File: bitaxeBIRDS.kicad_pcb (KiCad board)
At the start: 6 copper layers, 65 x 120 mm, 198 parts, among them J1 XT30, J4 Conn_01x04, Q1 BSS138, U12 TLV75512PDQNR, U14 TLV75512PDQNR, U15 TLV75512PDQNR, U2 TPS546D24SRVFR, U3 TLV75512PDQNR, U5 TPS22919DCKR, U8 SN74AXC4T774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

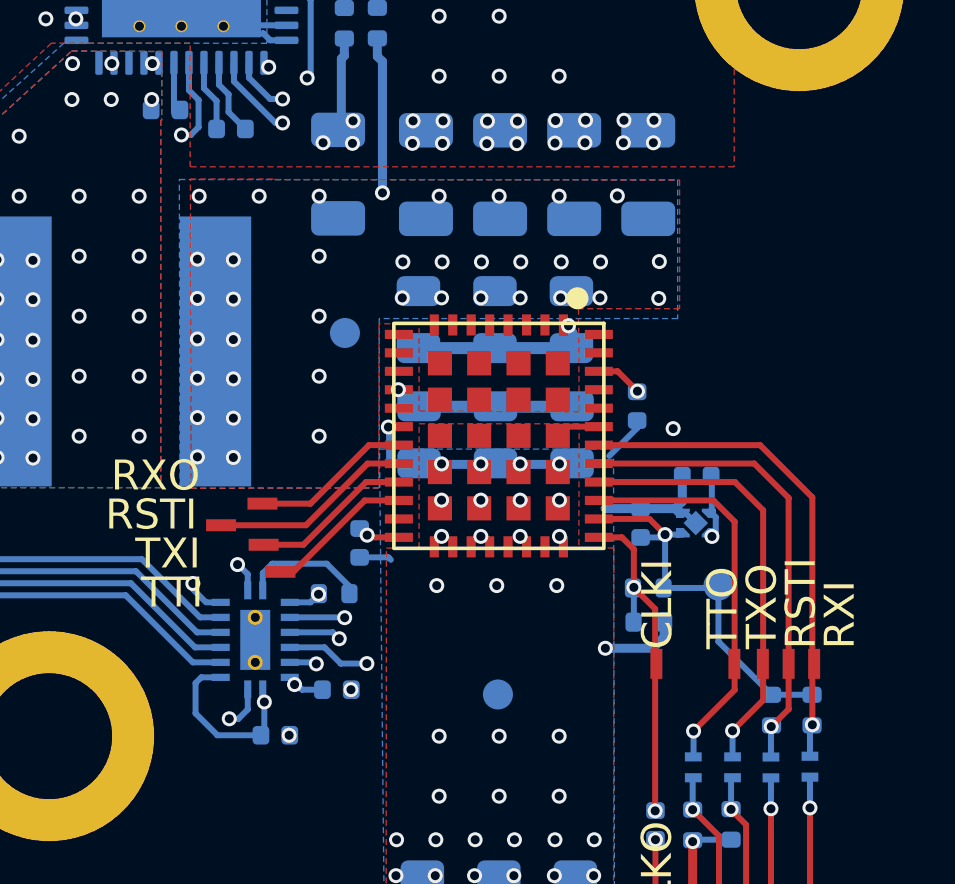
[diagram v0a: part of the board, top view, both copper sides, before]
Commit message: added pull resistors for #1
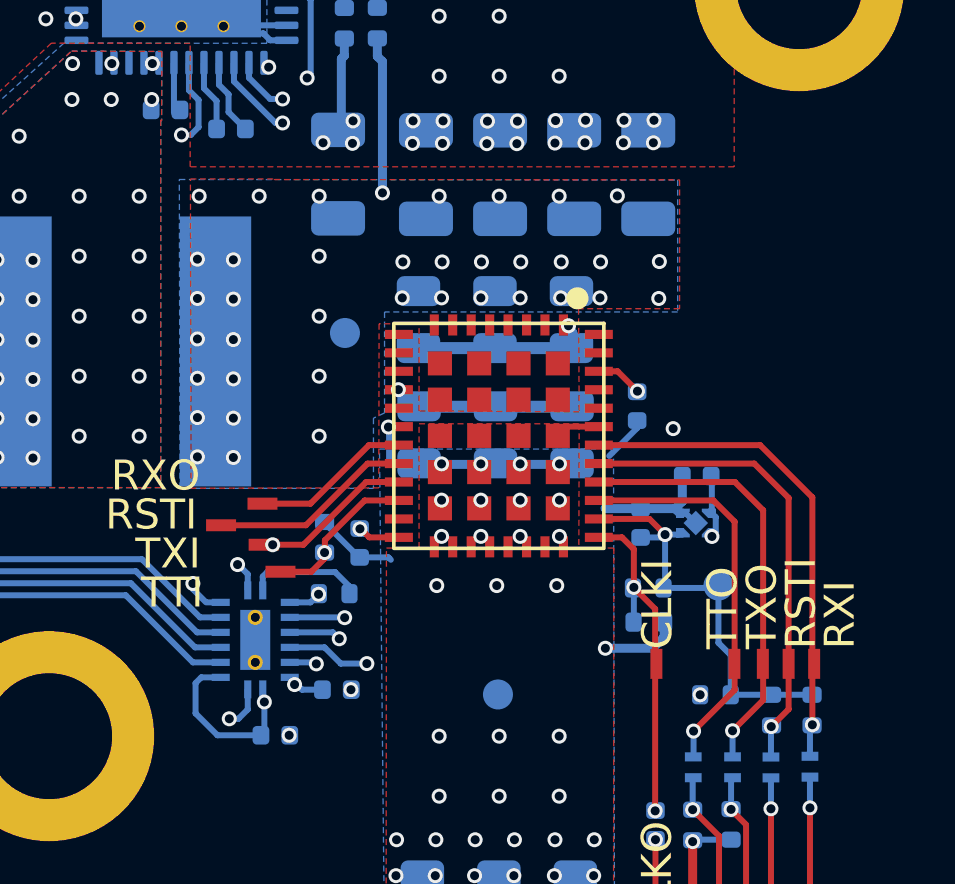
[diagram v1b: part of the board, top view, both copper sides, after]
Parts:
- added R4: 1k, Resistor_SMD:R_0402_1005Metric, B.Cu at (153.2, 110.6)
- added R9: 10k, Resistor_SMD:R_0402_1005Metric, B.Cu at (140.2, 105.4)
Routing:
- net Net-(A4-TX_IN): track 5.37 -> 24.8 mm, vias 0 -> 2
- net /ASIC/GND4: track 80.4 -> 82.1 mm
- net /ASIC/1V2-4: track 13.2 -> 14.0 mm
- net Net-(A4-TRIP_IN): track 4.93 -> 5.46 mm, vias 0 -> 1

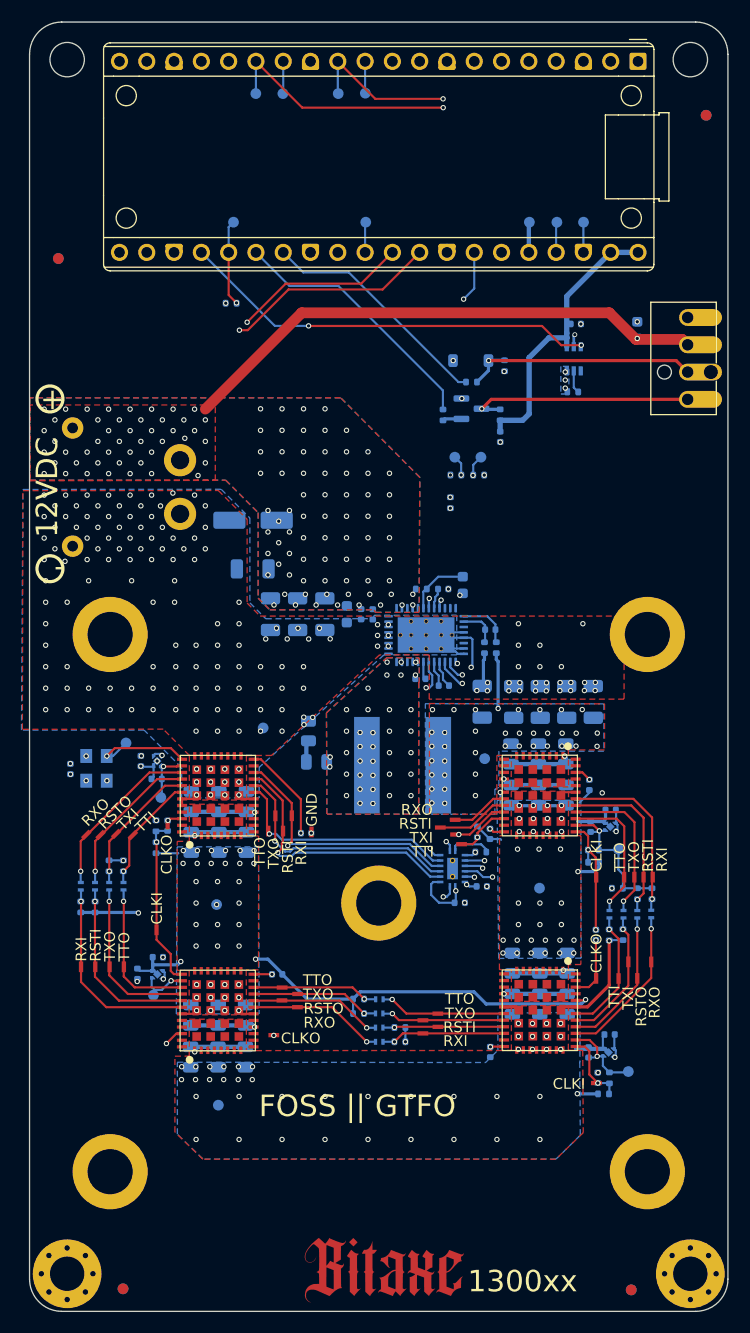
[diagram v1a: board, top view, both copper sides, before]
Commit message: changed all the level shifting diodes to SOD-523 packages for #6
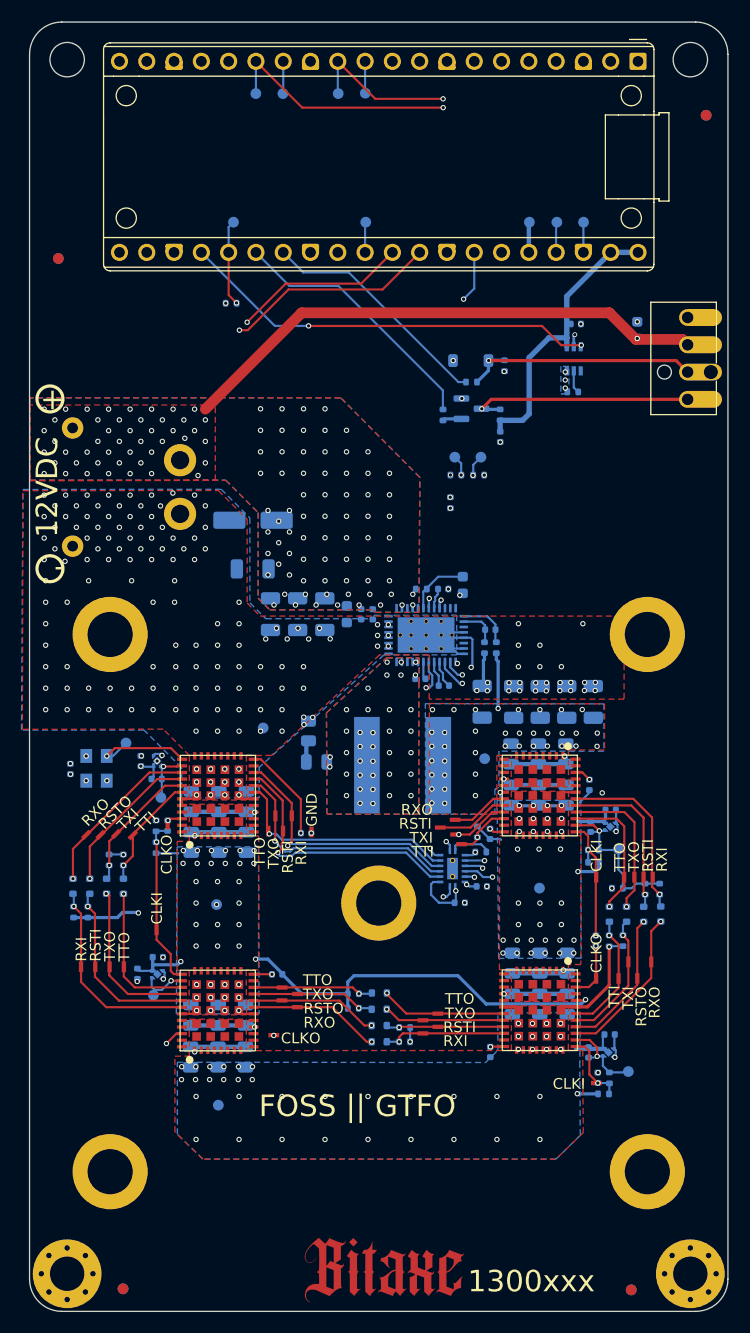
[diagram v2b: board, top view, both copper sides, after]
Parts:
- D1, D10, D11, D12, D2, D3, D4, D5, D6, D7, D8, D9: value DLLFSD01LPH4-7B -> DLLFSD01T-7; footprint bitaxe:DIODE_DLLFSD01LPH4-7B_DIO -> bitaxe:D_SOD-523
- moved D12 0.89 mm to (157.2, 113.0)
- moved R49 0.83 mm to (155.8, 110.7)
- moved R50 0.83 mm to (157.1, 110.7)
- moved R38 0.82 mm to (102.6, 112.8)
- moved R37 0.82 mm to (103.9, 112.8)
- moved D4 0.73 mm to (102.5, 110.4)
- moved R41 0.69 mm to (128.6, 120.4)
- moved R42 0.69 mm to (128.6, 121.8)
- moved D11 0.60 mm to (155.7, 113.0)
- moved D5 0.58 mm to (131.1, 120.4)
- moved R47 0.56 mm to (152.4, 115.5)
- moved R48 0.56 mm to (153.7, 115.5)
- moved R35 0.55 mm to (107.2, 108.0)
- moved R36 0.55 mm to (105.9, 108.0)
- moved C144 0.54 mm to (151.2, 115.5)
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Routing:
- net /ASIC/GND2: track 115.0 -> 116.5 mm
- net /ASIC/1V2-4: track 14.0 -> 14.9 mm
- net /ASIC/1V2-2: track 26.4 -> 27.3 mm
- net /ASIC/REFCLKOUT3: track 5.87 -> 5.18 mm
- net /ASIC/GND3: track 114.3 -> 113.7 mm
- net /ASIC/REFCLKIN4: track 11.5 -> 12.1 mm
- net /ASIC/shifter2-3/TX_IN: track 12.1 -> 11.6 mm
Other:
- board text added: "1300xxx"
- board text removed: "1300xx"

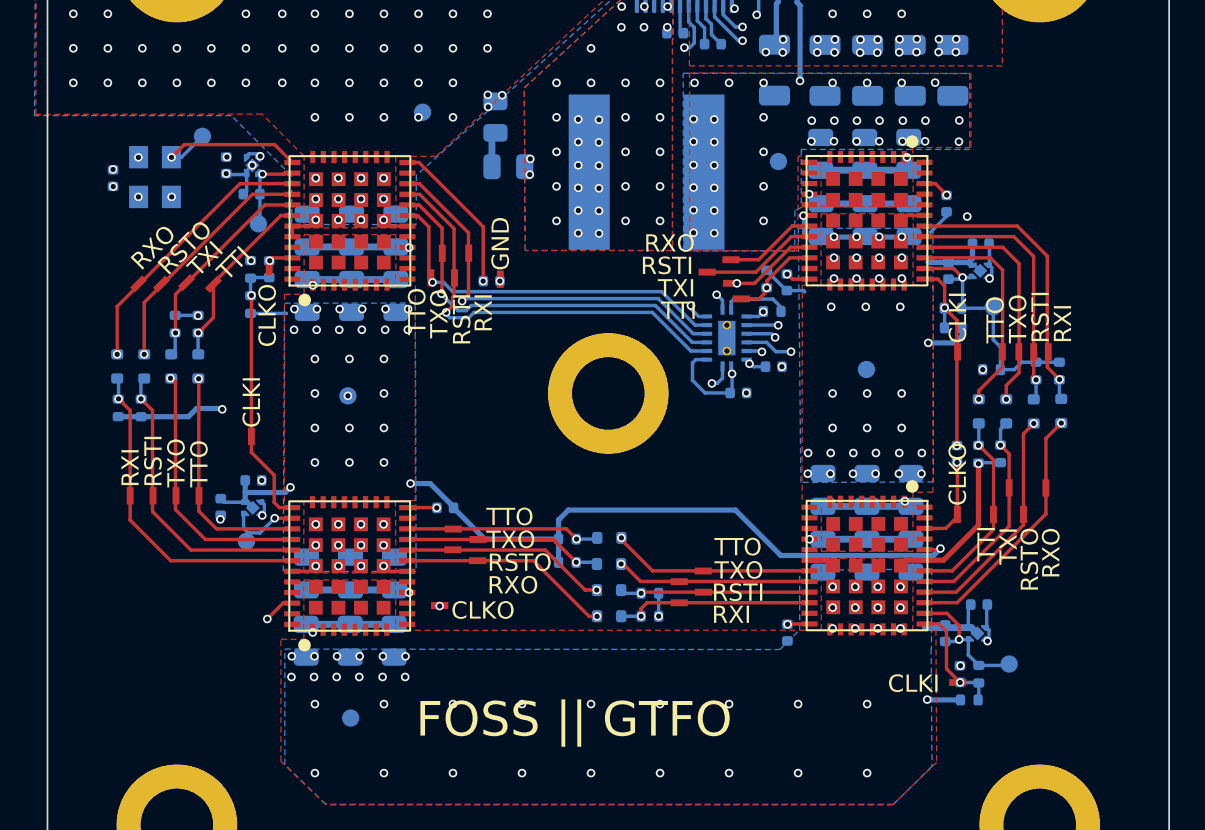
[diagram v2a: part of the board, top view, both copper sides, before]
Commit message: change IO voltage LDOs to bigger packages for #6
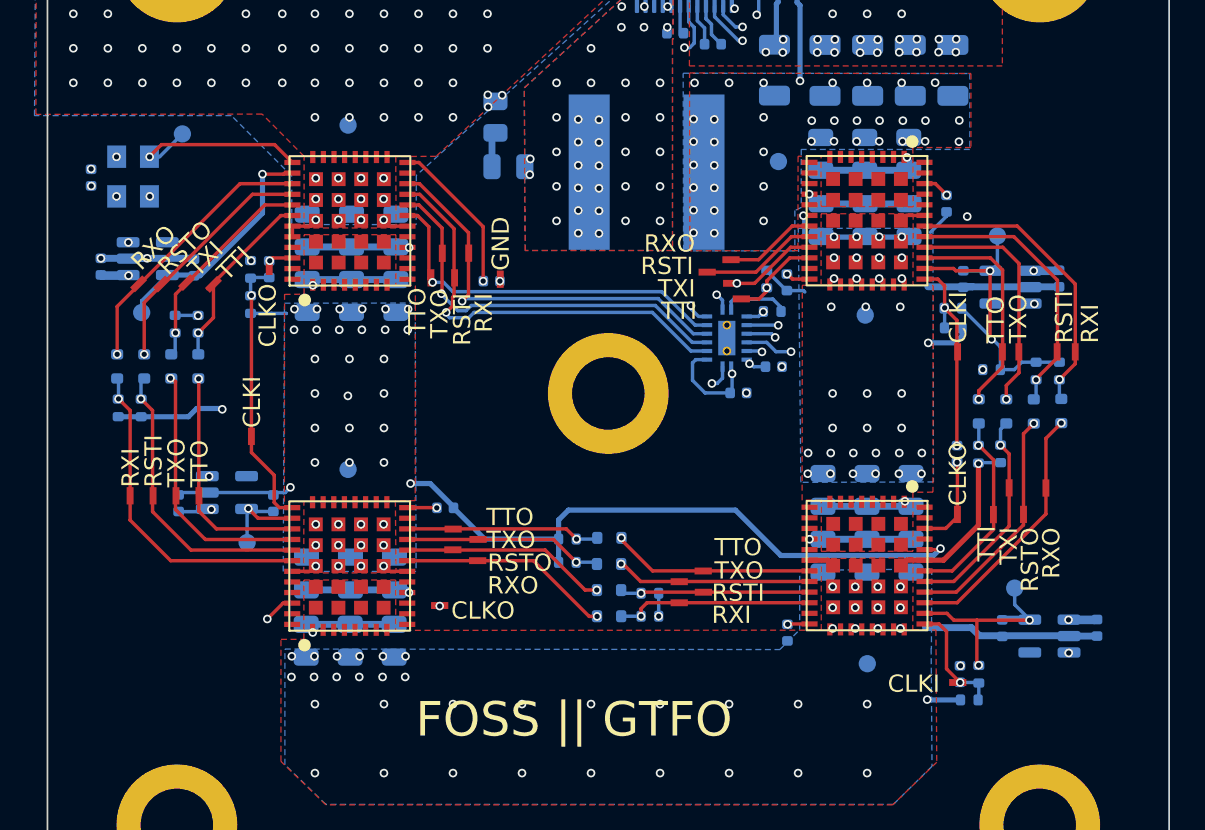
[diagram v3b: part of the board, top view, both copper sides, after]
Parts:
- removed U12, U14, U15: TLV75512PDQNR, bitaxe:DQN0004A
- added U1: MCP1824T-1202E/OT, Package_TO_SOT_SMD:SOT-23-5, B.Cu at (108.9, 117.7)
- added U4: MCP1824T-1202E/OT, Package_TO_SOT_SMD:SOT-23-5, B.Cu at (154.3, 105.8)
- added U6: MCP1824T-1202E/OT, Package_TO_SOT_SMD:SOT-23-5, B.Cu at (104.3, 104.2)
- U3: value TLV75512PDQNR -> MCP1824T-1202E/OT; footprint bitaxe:DQN0004A -> Package_TO_SOT_SMD:SOT-23-5
- moved U3 53.6 mm to (156.6, 126.1), turned to 180 degrees
- moved TP59 30.1 mm to (146.0, 127.7)
- moved C68 9.34 mm to (101.6, 104.7), turned to -90 degrees
- moved TP18 8.49 mm to (104.0, 107.3)
- moved C25 6.97 mm to (159.3, 125.6), turned to 90 degrees
- moved C72 5.41 mm to (107.0, 104.7), turned to -90 degrees
- moved C27 4.96 mm to (157.1, 105.3), turned to 90 degrees
- moved TP3 4.41 mm to (154.6, 123.3)
- moved TP19 4.38 mm to (115.9, 96.5)
- moved TP58 4.26 mm to (115.9, 116.4)
- moved TP4 4.12 mm to (153.6, 102.9)
- moved C26 3.32 mm to (153.8, 125.6), turned to 90 degrees
- moved TP60 3.15 mm to (145.9, 107.5)
- moved C7 2.45 mm to (106.1, 118.4)
- moved C19 1.75 mm to (111.6, 118.4), turned to -90 degrees
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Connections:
- U3 pad 1: /ASIC/1V2-1 -> /5V_SWITCH
- U3 pad 2: GND -> /ASIC/GND3
- U3 pad 4: /5V_SWITCH -> unconnected-(U3-PG-Pad4)
- U3 pad 5: GND -> /ASIC/1V2-3
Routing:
- net /5V_SWITCH: track 208.0 -> 189.5 mm, vias 9 -> 11
- net /ASIC/1V2-1: track 57.8 -> 68.3 mm
- net /ASIC/1V2-3: track 32.6 -> 38.9 mm, vias 2 -> 3
- net /ASIC/GND3: track 113.7 -> 118.9 mm
- net /ASIC/1V2-4: track 14.9 -> 19.8 mm, vias 1 -> 2
- net /ASIC/GND4: track 82.1 -> 85.6 mm
- net GND: track 31.0 -> 33.6 mm
- net /ASIC/REFCLKIN1: track 10.2 -> 11.6 mm
- net /ASIC/shifter3-4/RESET_IN: track 15.2 -> 16.3 mm
- net /ASIC/1V2-2: track 27.3 -> 28.3 mm, vias 4 -> 3
- net /ASIC/shifter3-4/RX_IN: track 16.4 -> 17.2 mm
- net /ASIC/GND2: track 116.5 -> 117.0 mm

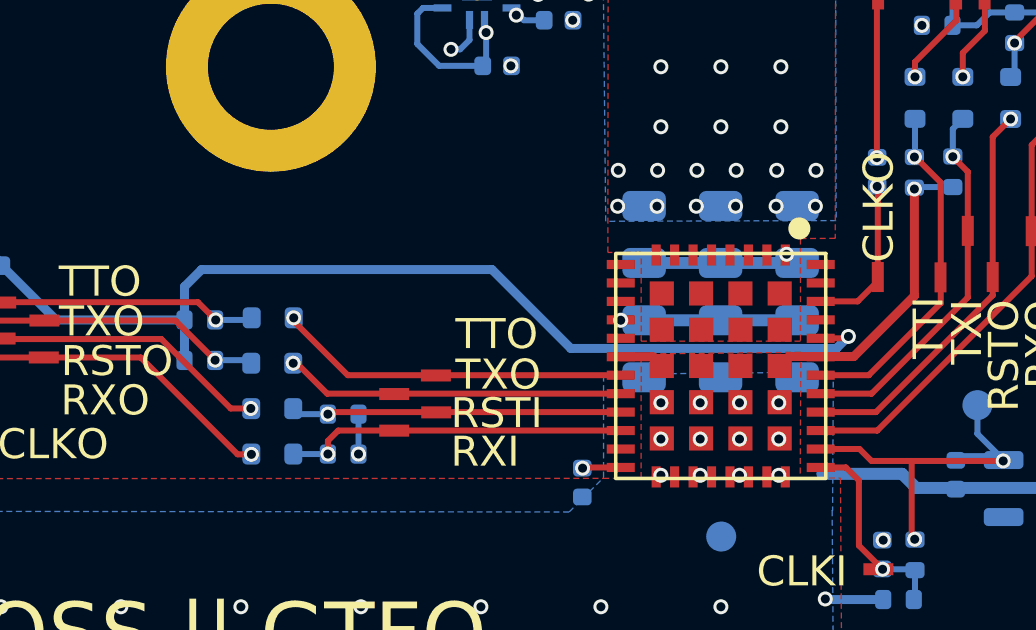
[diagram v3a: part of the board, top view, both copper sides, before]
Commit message: fix pinsel connection on ASIC 3 for #7
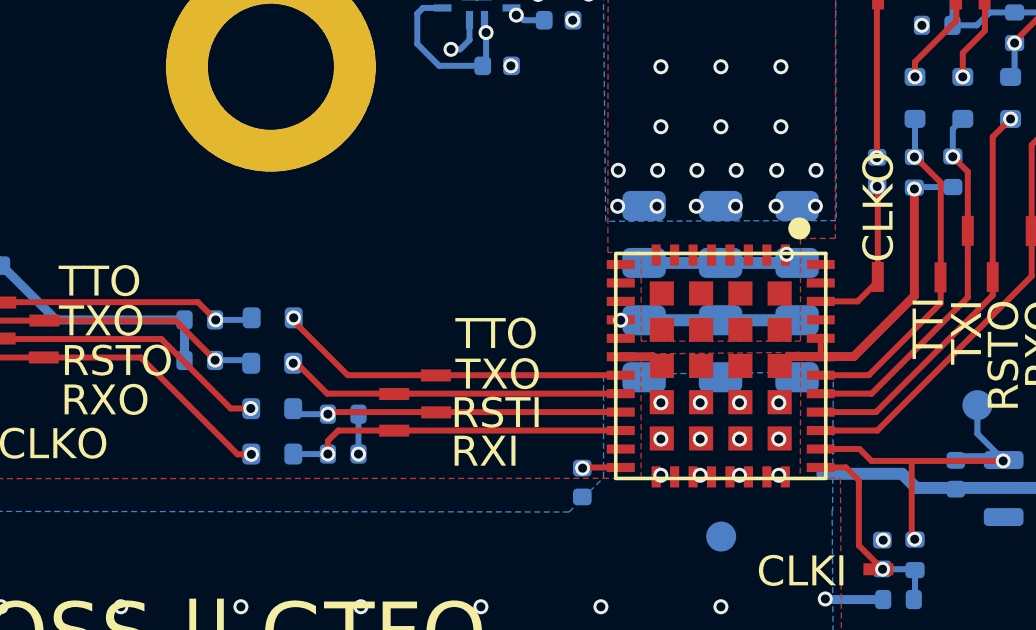
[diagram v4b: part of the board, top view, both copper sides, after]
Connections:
- A3 pad 36: /ASIC/GND2 -> /ASIC/GND3
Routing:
- net /ASIC/GND2: track 117.0 -> 91.3 mm, vias 40 -> 39
- net /ASIC/GND3: track 118.9 -> 119.5 mm
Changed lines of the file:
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@@
 			(size 0.305 0.935)
 			(layers "F.Cu" "F.Mask" "F.Paste")
-			(net 38 "/ASIC/GND2")
+			(net 3 "/ASIC/GND3")
 			(pinfunction "PINSEL")
 			(pintype "unspecified")
@@
 	)
 	(segment
+		(start 149.3275 121.052)
+		(end 149.3275 121.667)
+		(width 0.2)
+		(layer "F.Cu")
+		(net 3)
+	)
+	(segment
 		(start 118.03 58.68)
 		(end 118.81 58.68)
@@
 	)
 	(segment
-		(start 150.188 121.052)
-		(end 150.25 120.99)
-		(width 0.2)
-		(layer "F.Cu")
-		(net 38)
-	)
-	(segment
 		(start 129.36 54.35)
 		(end 132.27 51.44)
@@
 	)
 	(segment
-		(start 149.3275 121.052)
-		(end 150.188 121.052)
-		(width 0.2)
-		(layer "F.Cu")
-		(net 38)
-	)
-	(segment
 		(start 119.3475 122.307)
 		(end 118.287 122.307)
@@
 	)
 	(via
-		(at 150.25 120.99)
-		(size 0.5)
-		(drill 0.3)
-		(layers "F.Cu" "B.Cu")
-		(net 38)
-	)
-	(via
 		(at 118 110)
 		(size 0.5)
@@
 	)
 	(segment
-		(start 150.25 120.99)
-		(end 149.85 121.39)
-		(width 0.3)
-		(layer "B.Cu")
-		(net 38)
-	)
-	(segment
-		(start 140.99813 121.39)
-		(end 138.36813 118.76)
-		(width 0.3)
-		(layer "B.Cu")
-		(net 38)
-	)
-	(segment
 		(start 111.48 107.36)
 		(end 112.33 107.36)
@@
 	(segment
 		(start 128.12 120.44)
+		(end 128.12 121.79)
+		(width 0.3)
+		(layer "B.Cu")
+		(net 38)
+	)
+	(segment
+		(start 128.12 120.44)
 		(end 123.84 120.44)
 		(width 0.3)
@@
 	)
 	(segment
-		(start 149.85 121.39)
-		(end 140.99813 121.39)
-		(width 0.3)
-		(layer "B.Cu")
-		(net 38)
-	)
-	(segment
 		(start 110.27 107.36)
 		(end 111.48 107.36)
@@
 		(layer "B.Cu")
 		(net 38)
-	)
-	(segment
-		(start 128.69 118.76)
-		(end 128.12 119.33)
-		(width 0.3)
-		(layer "B.Cu")
-		(net 38)
-	)
-	(segment
-		(start 138.36813 118.76)
-		(end 128.69 118.76)
-		(width 0.3)
-		(layer "B.Cu")
-		(net 38)
-	)
-	(segment
-		(start 128.12 119.33)
-		(end 128.12 121.79)
-		(width 0.3)
-		(layer "B.Cu")
-		(net 38)
